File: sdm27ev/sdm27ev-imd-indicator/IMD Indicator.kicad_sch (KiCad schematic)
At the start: 14 parts, among them J5 776280-1, Q1 2N7002,215, Q2 2N7002,215

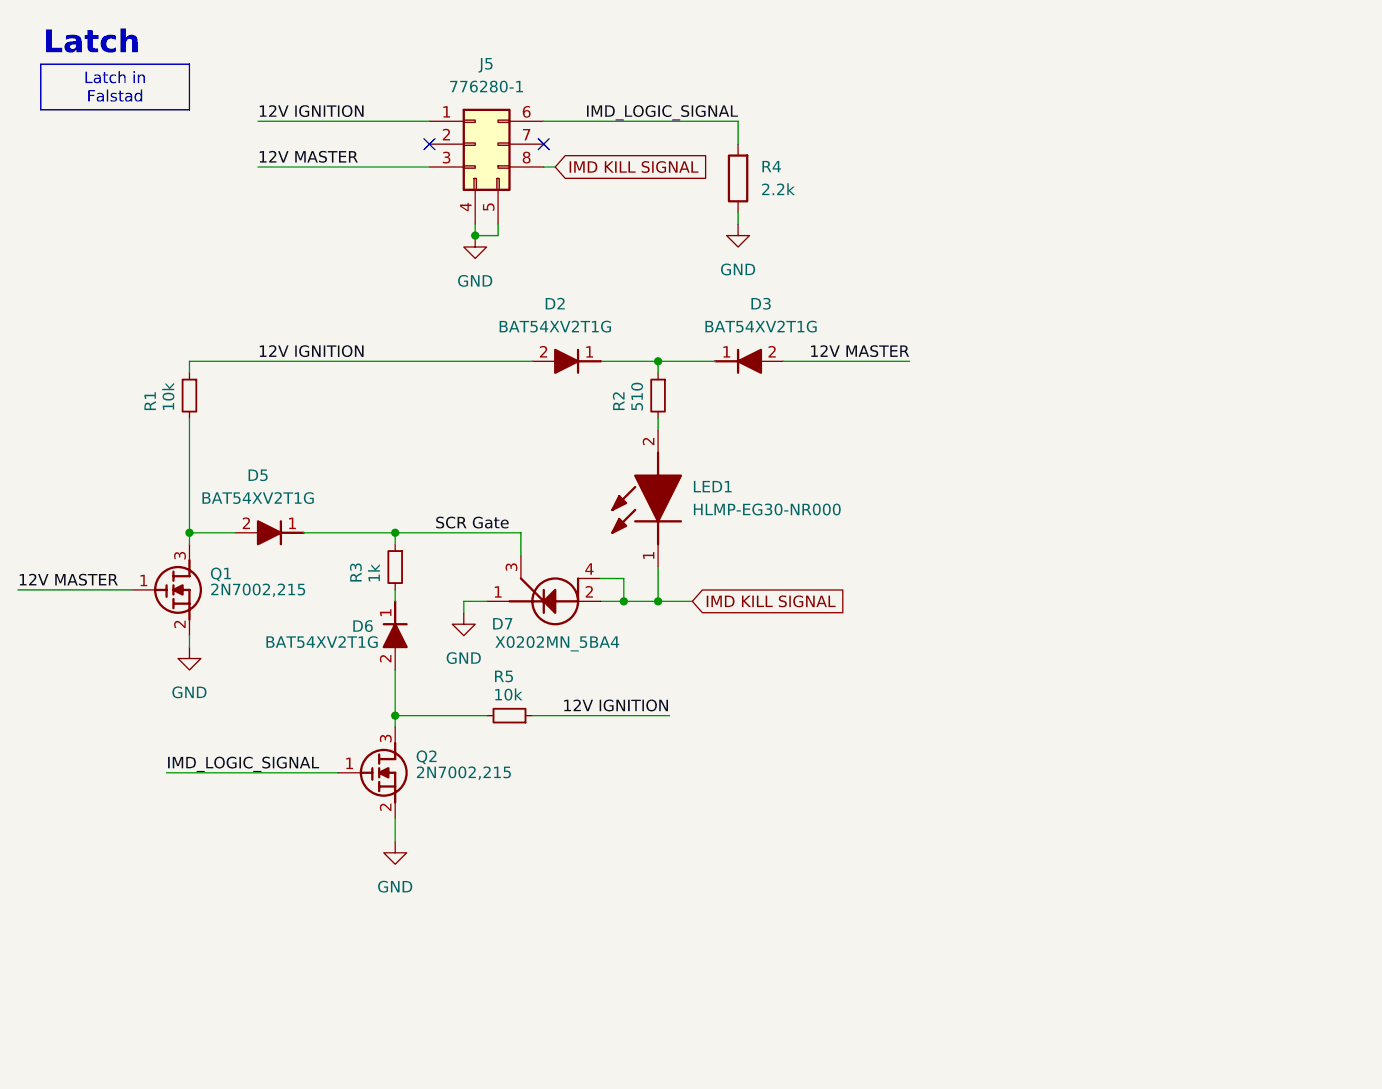
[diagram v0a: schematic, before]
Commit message: Changed IMD to only account for master, not ignition (still need to do layout and LED connector)
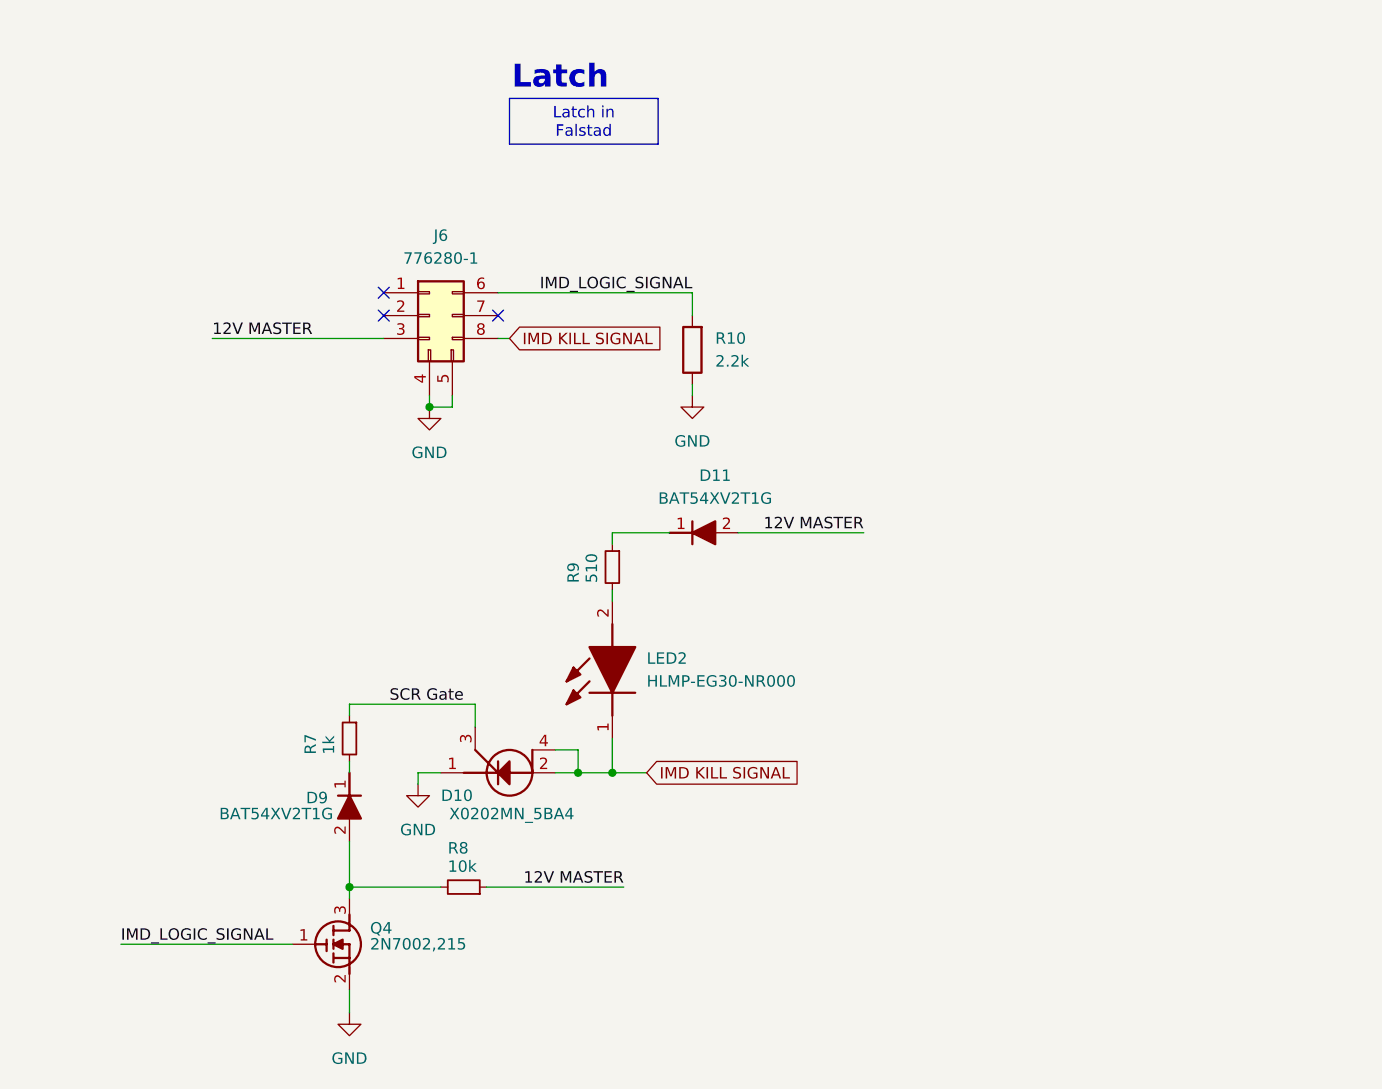
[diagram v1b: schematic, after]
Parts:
- removed D2, D3, D5, D6: BAT54XV2T1G, SDM_MiscFootprint:SODFL1608X70N, symbol SDM_DIODES:BAT54XV2T1G
- removed D7: X0202MN_5BA4, SDM_MiscFootprint:SOT230P700X190-4N, symbol SDM_SCR:X0202MN_5BA4
- removed J5: 776280-1, SDM_MiscFootprint:776280-1, symbol IMDSymbolLibrary:776280-1
- removed LED1: HLMP-EG30-NR000, IMDFootprintLibrary:LED_5MM, symbol IMDSymbolLibrary:HLMP-EG30-NR000
- removed Q1, Q2: 2N7002,215, SDM_MiscFootprint:SOT95P230X110-3N, symbol SDM_MOSFET_N-CHANNEL:2N7002,215
- removed R1, R5: 10k, Resistor_SMD:R_0603_1608Metric, symbol Device:R_Small
- removed R2: 510, Resistor_SMD:R_0603_1608Metric, symbol Device:R_Small
- removed R3: 1k, Resistor_SMD:R_0603_1608Metric, symbol Device:R_Small
- removed R4: 2.2k, Resistor_SMD:R_0603_1608Metric, symbol Device:R
- added D10: X0202MN_5BA4, SDM_MiscFootprint:SOT230P700X190-4N, symbol SDM_SCR:X0202MN_5BA4
- added D11, D9: BAT54XV2T1G, SDM_MiscFootprint:SODFL1608X70N, symbol SDM_DIODES:BAT54XV2T1G
- added J6: 776280-1, SDM_MiscFootprint:776280-1, symbol IMDSymbolLibrary:776280-1
- added LED2: HLMP-EG30-NR000, IMDFootprintLibrary:LED_5MM, symbol IMDSymbolLibrary:HLMP-EG30-NR000
- added Q4: 2N7002,215, SDM_MiscFootprint:SOT95P230X110-3N, symbol SDM_MOSFET_N-CHANNEL:2N7002,215
- added R10: 2.2k, Resistor_SMD:R_0603_1608Metric, symbol Device:R
- added R7: 1k, Resistor_SMD:R_0603_1608Metric, symbol Device:R_Small
- added R8: 10k, Resistor_SMD:R_0603_1608Metric, symbol Device:R_Small
- added R9: 510, Resistor_SMD:R_0603_1608Metric, symbol Device:R_Small
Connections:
- net 12V MASTER: now also D11.2 (A), J6.3 (Pin_3), R8.1
- net GND: now also D10.1 (K), J6.4 (Pin_4), J6.5 (Pin_5), Q4.2 (S), R10.1
- net IMD KILL SIGNAL: now also D10.2 (A_1), D10.4 (A_2), J6.8 (Pin_8), LED2.1 (K)
- net IMD_LOGIC_SIGNAL: now also J6.6 (Pin_6), Q4.1 (G), R10.2
- net SCR Gate: now also D10.3 (G), R7.1
- new net: LED2.2 (A), R9.2
- new net: D9.1 (K), R7.2
- new net: D9.2 (A), Q4.3 (D), R8.2
- new net: D11.1 (K), R9.1
- no-connect marks 2 -> 3

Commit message: imd initial LED connector and lamp test
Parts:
- removed LED2: HLMP-EG30-NR000, IMDFootprintLibrary:LED_5MM, symbol IMDSymbolLibrary:HLMP-EG30-NR000
- added J1: Conn_01x02_Socket, Connector_Molex:Molex_Micro-Fit_3.0_43045-0215_2x01_P3.00mm_Vertical, symbol Connector:Conn_01x02_Socket
- added Q5: 2N7002,215, SDM_MiscFootprint:SOT95P230X110-3N, symbol SDM_MOSFET_N-CHANNEL:2N7002,215
- added R11: 1k, Resistor_SMD:R_0603_1608Metric, symbol Device:R_Small
- added R12: 100k, Resistor_SMD:R_0603_1608Metric, symbol Device:R_Small
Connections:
- net GND: now also Q5.2 (S), R12.2
- net IMD KILL SIGNAL: now also J1.2 (Pin_2), Q5.3 (D)
- net LAMP_TEST: now reaches J6.1 (Pin_1)
- net LAMP_TEST: now also R11.1
- net at R9.2: now also J1.1 (Pin_1)
- new net: Q5.1 (G), R11.2, R12.1
- no-connect marks 3 -> 2
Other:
- note added: "LED is HLMP-EG30-NR000"
- note added: "top pin is led anode connection bottom pin is led cathode connection"

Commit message: IMD updated lamp test
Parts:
- added D1: 1N4148, Diode_THT:D_DO-35_SOD27_P7.62mm_Horizontal, symbol Diode:1N4148
- added Q1: BSS84, Package_TO_SOT_SMD:SOT-23, symbol Transistor_FET:BSS84
- added R13: 1k, Resistor_SMD:R_0603_1608Metric, symbol Device:R_Small
- added R14: 100k, Resistor_SMD:R_0603_1608Metric, symbol Device:R_Small
- R11: value 1k -> 47k
- R12: value 100k -> 560
- R9: value 510 -> 620
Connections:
- net GND: now also J1.2 (Pin_2), R14.1; no longer R12.2
- net IMD KILL SIGNAL: now also R11.1, R9.2; no longer J1.2 (Pin_2), Q5.3 (D)
- net LAMP_TEST: now also R13.1; no longer R11.1
- net at J1.1 (Pin_1): now also R12.2; no longer R9.2
- net at D11.1 (K), R9.1: now also D1.2 (A)
- new net: Q1.1 (G), Q5.3 (D), R11.2
- new net: D1.1 (K), Q1.2 (S)
- new net: Q1.3 (D), R12.1
- new net: Q5.1 (G), R13.2, R14.2
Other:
- moved on the sheet: J1

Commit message: IMD temp push for BOM
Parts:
- removed J1: Conn_01x02_Socket, Connector_Molex:Molex_Micro-Fit_3.0_43045-0215_2x01_P3.00mm_Vertical, symbol Connector:Conn_01x02_Socket
- D1: footprint Diode_THT:D_DO-35_SOD27_P7.62mm_Horizontal -> Diode_SMD:D_SOD-123
- J6: footprint SDM_MiscFootprint:776280-1 -> IMDFootprintLibrary:776280-1
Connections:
- net GND: now also J6.2 (Pin_2)
- net LAMP_TEST: now also J6.7 (Pin_7); no longer J6.1 (Pin_1)
- net LED+: now reaches R12.2
- net LED+: now also J6.1 (Pin_1)
- no-connect marks 2 -> 0
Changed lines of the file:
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@@
 		(color 0 0 0 0)
 	)
-	(no_connect
-		(at 120.65 67.31)
-	)
-	(no_connect
-		(at 133.35 67.31)
-	)
 	(wire
 		(pts
@@
 	(wire
 		(pts
-			(xy 101.6 64.77) (xy 120.65 64.77)
-		)
-		(stroke
-			(width 0)
-			(type default)
-		)
-	)
-	(wire
-		(pts
 			(xy 187.96 120.65) (xy 173.99 120.65)
 		)
@@
 	(wire
 		(pts
+			(xy 111.76 64.77) (xy 120.65 64.77)
+		)
+		(stroke
+			(width 0)
+			(type default)
+		)
+	)
+	(wire
+		(pts
 			(xy 154.94 74.93) (xy 154.94 76.2)
 		)
@@
 	(wire
 		(pts
+			(xy 133.35 67.31) (xy 138.43 67.31)
+		)
+		(stroke
+			(width 0)
+			(type default)
+		)
+	)
+	(wire
+		(pts
 			(xy 142.24 118.11) (xy 142.24 115.57)
 		)
@@
 	(wire
 		(pts
+			(xy 111.76 67.31) (xy 120.65 67.31)
+		)
+		(stroke
+			(width 0)
+			(type default)
+		)
+	)
+	(wire
+		(pts
 			(xy 146.05 91.44) (xy 152.4 91.44)
 		)
@@
 		)
 	)
-	(label "LAMP_TEST"
-		(at 101.6 64.77 0)
+	(label "LED+"
+		(at 111.76 64.77 180)
 		(effects
 			(font
 				(size 1.27 1.27)
 			)
-			(justify left bottom)
+			(justify right bottom)
 		)
 	)
@@
 		)
 	)
+	(label "LED+"
+		(at 201.93 97.79 0)
+		(effects
+			(font
+				(size 1.27 1.27)
+			)
+			(justify left bottom)
+		)
+	)
+	(label "LED-"
+		(at 111.76 67.31 180)
+		(effects
+			(font
+				(size 1.27 1.27)
+			)
+			(justify right bottom)
+		)
+	)
 	(label "IMD_LOGIC_SIGNAL"
 		(at 91.44 137.16 0)
@@
 			)
 			(justify right bottom)
+		)
+	)
+	(label "LED-"
+		(at 201.93 100.33 0)
+		(effects
+			(font
+				(size 1.27 1.27)
+			)
+			(justify left bottom)
+		)
+	)
+	(label "LAMP_TEST"
+		(at 138.43 67.31 0)
+		(effects
+			(font
+				(size 1.27 1.27)
+			)
+			(justify left bottom)
 		)
 	)
@@
 			)
 		)
-		(property "Footprint" "SDM_MiscFootprint:776280-1"
+		(property "Footprint" "IMDFootprintLibrary:776280-1"
 			(at 137.16 159.69 0)
 			(hide yes)
@@
 			)
 		)
-		(property "Datasheet" "https://www.te.com/commerce/DocumentDelivery/DDEController?Action=srchrtrv&DocNm=776280&DocType=Customer+Drawing&DocLang=English&PartCntxt=776280-1&DocFormat=pdf"
+		(property "Datasheet" "https://www.te.com/commerce/DocumentDelivery/DDEController?Action=srchrtrv&DocNm=1-1773979-2&DocType=Data%20Sheet&DocLang=English&PartCntxt=776280-1&DocFormat=pdf"
 			(at 137.16 259.69 0)
 			(hide yes)
@@
 	)
 	(symbol
-		(lib_id "Connector:Conn_01x02_Socket")
-		(at 207.01 97.79 0)
-		(unit 1)
-		(body_style 1)
-		(exclude_from_sim no)
-		(in_bom yes)
-		(on_board yes)
-		(in_pos_files yes)
-		(dnp no)
-		(fields_autoplaced yes)
-		(property "Reference" "J1"
-			(at 208.28 97.7899 0)
-			(show_name no)
-			(do_not_autoplace no)
-			(effects
-				(font
-					(size 1.27 1.27)
-				)
-				(justify left)
-			)
-		)
-		(property "Value" "Conn_01x02_Socket"
-			(at 208.28 100.3299 0)
-			(show_name no)
-			(do_not_autoplace no)
-			(effects
-				(font
-					(size 1.27 1.27)
-				)
-				(justify left)
-			)
-		)
-		(property "Footprint" "Connector_Molex:Molex_Micro-Fit_3.0_43045-0215_2x01_P3.00mm_Vertical"
-			(at 207.01 97.79 0)
-			(hide yes)
-			(show_name no)
-			(do_not_autoplace no)
-			(effects
-				(font
-					(size 1.27 1.27)
-				)
-			)
-		)
-		(property "Datasheet" ""
-			(at 207.01 97.79 0)
-			(hide yes)
-			(show_name no)
-			(do_not_autoplace no)
-			(effects
-				(font
-					(size 1.27 1.27)
-				)
-			)
-		)
-		(property "Description" "Generic connector, single row, 01x02, script generated"
-			(at 207.01 97.79 0)
-			(hide yes)
-			(show_name no)
-			(do_not_autoplace no)
-			(effects
-				(font
-					(size 1.27 1.27)
-				)
-			)
-		)
-		(pin "2"
-		)
-		(pin "1"
-		)
-		(instances
-			(project "IMD Indicator"
-				(path "/2d398882-e4dd-424e-9a5b-db438ffb0a84"
-					(reference "J1")
-					(unit 1)
-				)
-			)
-		)
-	)
-	(symbol
 		(lib_id "power:GND")
 		(at 116.84 144.78 0)
@@
 			)
 		)
-		(property "Footprint" "Diode_THT:D_DO-35_SOD27_P7.62mm_Horizontal"
+		(property "Footprint" "Diode_SMD:D_SOD-123"
 			(at 152.4 96.52 0)
 			(hide yes)

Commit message: IMD complete
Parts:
- removed D1: 1N4148, Diode_SMD:D_SOD-123, symbol Diode:1N4148
- added D1: LED, LED_SMD:LED_0805_2012Metric, symbol Device:LED
- added TP1: GND_TEST, TestPoint:TestPoint_Pad_D1.5mm, symbol Connector:TestPoint
- added TP2: LED_TEST, TestPoint:TestPoint_Pad_D1.5mm, symbol Connector:TestPoint
- added TP3: KILL_TEST, TestPoint:TestPoint_Pad_D1.5mm, symbol Connector:TestPoint
- added TP4: SCR_TEST, TestPoint:TestPoint_Pad_D1.5mm, symbol Connector:TestPoint
- added TP5: Q4_TEST, TestPoint:TestPoint_Pad_D1.5mm, symbol Connector:TestPoint
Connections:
- net GND: now also TP1.1
- net IMD KILL SIGNAL: now also TP3.1
- net SCR Gate: now also TP4.1
- net at Q1.1 (G), Q5.3 (D), R11.2: now also TP2.1
- net at Q1.2 (S): now also D1.1 (K)
- net at D9.2 (A), Q4.3 (D), R8.2: now also TP5.1
- net at D11.1 (K), R9.1: now also D1.2 (A)
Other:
- note removed: "top pin is led anode connection bottom pin is led cathode connection"
